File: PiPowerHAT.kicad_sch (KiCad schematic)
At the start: 34 parts

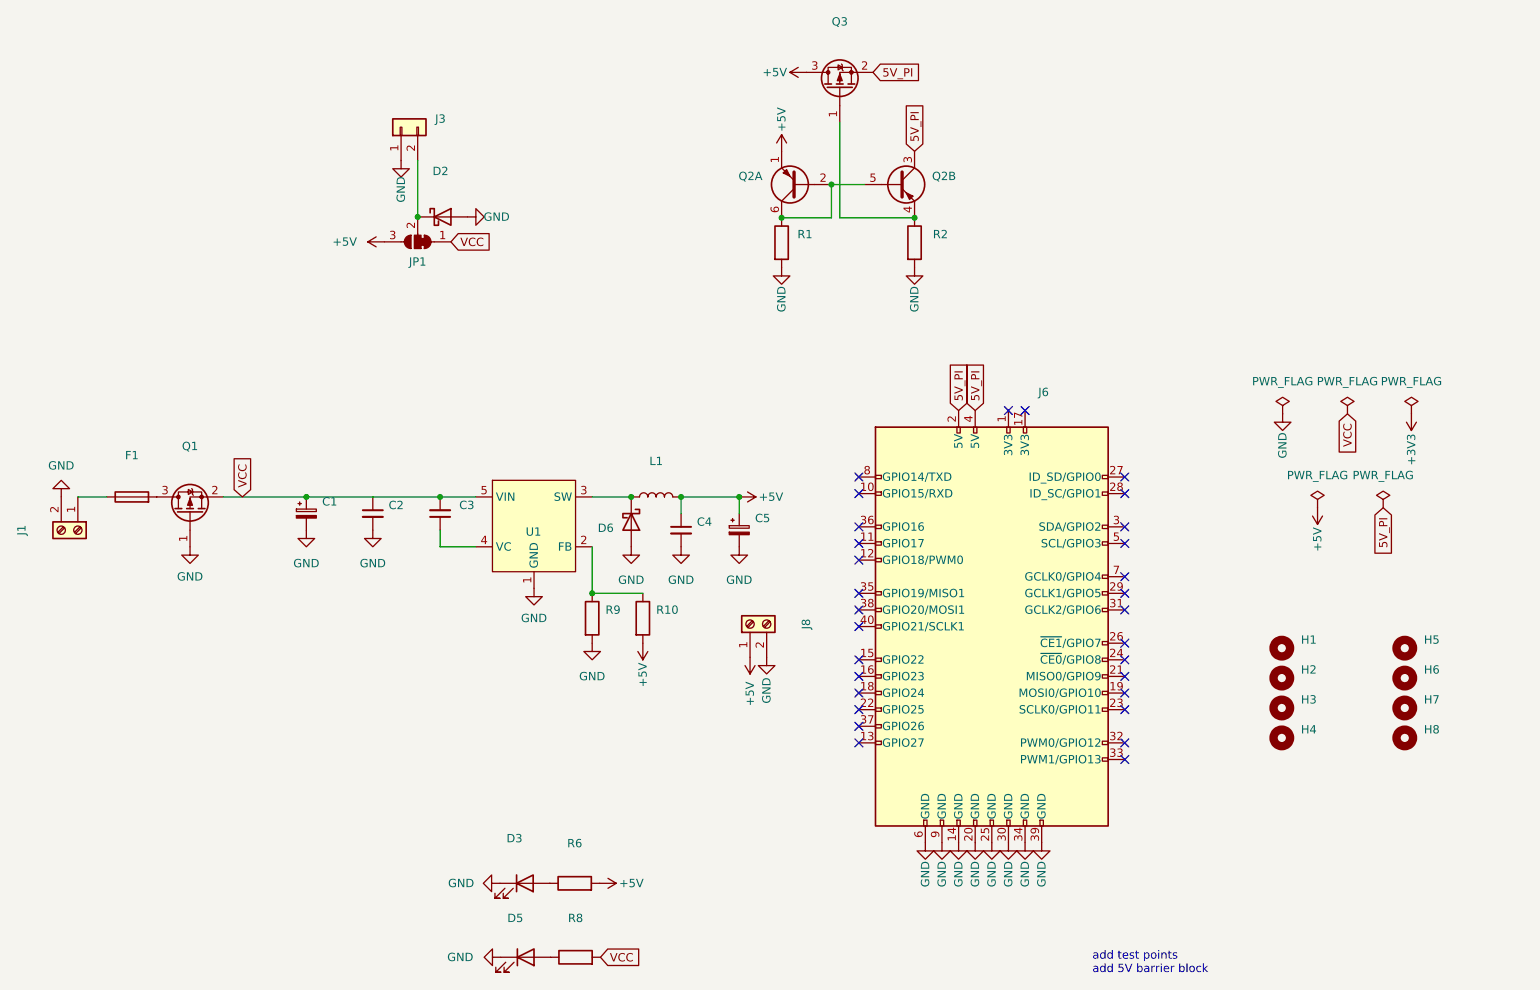
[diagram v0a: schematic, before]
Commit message: Part Numbers for Littelfuse removed.
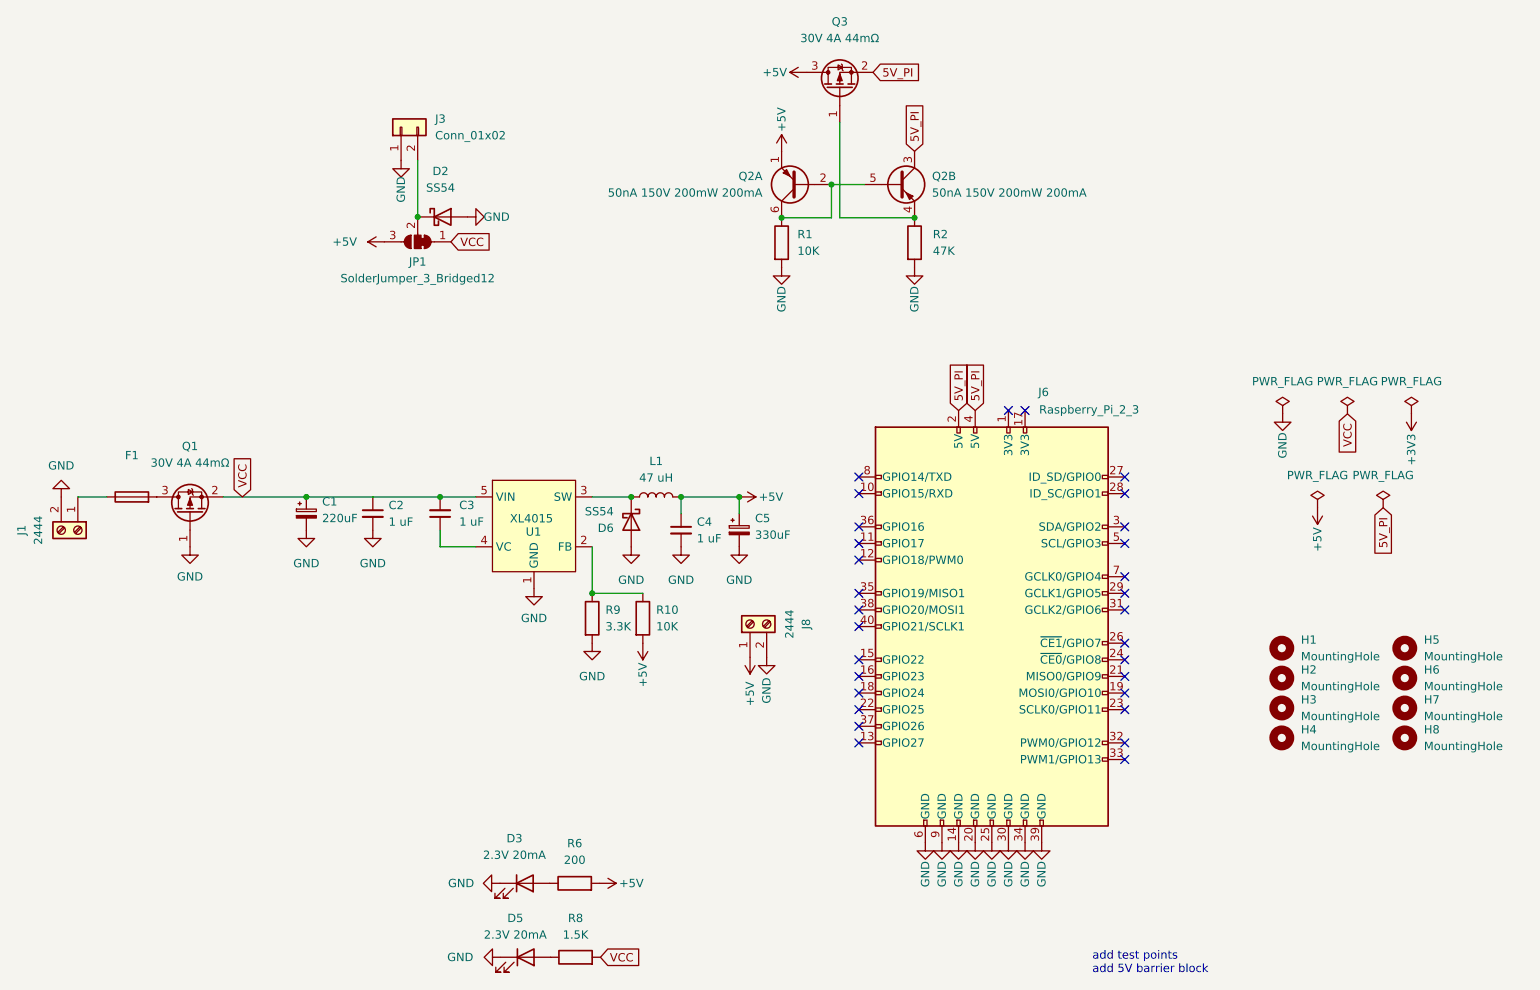
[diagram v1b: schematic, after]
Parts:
- C1: value (none) -> 220uF; footprint (none) -> Capacitor_SMD:CP_Elec_10x10
- C2, C3, C4: value (none) -> 1 uF; footprint (none) -> Capacitor_SMD:C_0603_1608Metric
- C5: value (none) -> 330uF; footprint (none) -> Capacitor_SMD:CP_Elec_6.3x7.7
- D2, D6: value (none) -> SS54; footprint (none) -> Diode_SMD:D_SMA
- D3, D5: value (none) -> 2.3V 20mA; footprint (none) -> LED_SMD:LED_0603_1608Metric
- F1: LCSC C206916 -> (none); PCBway 0154005.DR -> (none)
- H1, H2, H3, H4: value (none) -> MountingHole; footprint (none) -> MountingHole:MountingHole_2.7mm_M2.5_DIN965_Pad
- H5, H6, H7, H8: value (none) -> MountingHole; footprint (none) -> MountingHole:MountingHole_3.5mm
- J1: value (none) -> 2444; footprint (none) -> TerminalBlock_4Ucon:TerminalBlock_4Ucon_1x02_P3.50mm_Horizontal
- J3: value (none) -> Conn_01x02; footprint (none) -> Connector_JST:JST_XH_B2B-XH-A_1x02_P2.50mm_Vertical
- J6: value (none) -> Raspberry_Pi_2_3; footprint (none) -> Connector_PinSocket_2.54mm:PinSocket_2x20_P2.54mm_Vertical
- J8: value (none) -> 2444; footprint (none) -> Connector_JST:JST_XH_B2B-XH-A_1x02_P2.50mm_Vertical
- JP1: value (none) -> SolderJumper_3_Bridged12; footprint (none) -> Jumper:SolderJumper-3_P1.3mm_Bridged2Bar12_RoundedPad1.0x1.5mm
- L1: value (none) -> 47 uH; footprint (none) -> Inductor_SMD:L_12x12mm_H6mm
- Q1, Q3: value (none) -> 30V 4A 44mΩ; footprint (none) -> Package_TO_SOT_SMD:SOT-23
- Q2: value (none) -> 50nA 150V 200mW 200mA; footprint (none) -> Package_TO_SOT_SMD:SOT-363_SC-70-6
- R1: value (none) -> 10K; footprint (none) -> Resistor_SMD:R_0402_1005Metric
- R10: value (none) -> 10K; footprint (none) -> Resistor_SMD:R_0603_1608Metric
- R2: value (none) -> 47K; footprint (none) -> Resistor_SMD:R_0402_1005Metric
- R6: value (none) -> 200; footprint (none) -> Resistor_SMD:R_0402_1005Metric
- R8: value (none) -> 1.5K; footprint (none) -> Resistor_SMD:R_0402_1005Metric
- R9: value (none) -> 3.3K; footprint (none) -> Resistor_SMD:R_0603_1608Metric
- U1: value (none) -> XL4015; footprint (none) -> Package_TO_SOT_SMD:TO-263-5_TabPin3

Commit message: bug fixes
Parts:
- F1: value (none) -> 5A; footprint (none) -> Fuse:Fuseholder_Blade_Mini_Keystone_3568
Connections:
- net 5V_PI: now also Q2.4 (E2); no longer Q2.3 (C2)
- net VCC: now also C2.1
- net at Q3.1 (G), R2.1: now also Q2.3 (C2); no longer Q2.4 (E2)
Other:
- moved on the sheet: Q2B
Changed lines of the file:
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@@
 (kicad_sch (version 20211123) (generator eeschema)
   (paper "A4")
+  (junction (at 137.795 47.879) (diameter 0) (color 0 0 0 0)
+  )
   (junction (at 77.978 95.631) (diameter 0) (color 0 0 0 0)
   )
+  (junction (at 67.7164 95.631) (diameter 0) (color 0 0 0 0)
+  )
   (junction (at 57.531 95.631) (diameter 0) (color 0 0 0 0)
   )
+  (junction (at 107.188 95.631) (diameter 0) (color 0 0 0 0)
+  )
+  (junction (at 114.808 95.631) (diameter 0) (color 0 0 0 0)
+  )
+  (junction (at 123.698 95.631) (diameter 0) (color 0 0 0 0)
+  )
   (junction (at 150.495 52.959) (diameter 0) (color 0 0 0 0)
   )
-  (junction (at 107.188 95.631) (diameter 0) (color 0 0 0 0)
-  )
-  (junction (at 114.808 95.631) (diameter 0) (color 0 0 0 0)
-  )
-  (junction (at 123.698 95.631) (diameter 0) (color 0 0 0 0)
-  )
   (junction (at 130.175 52.959) (diameter 0) (color 0 0 0 0)
-  )
-  (junction (at 137.795 47.879) (diameter 0) (color 0 0 0 0)
   )
   (junction (at 101.219 110.363) (diameter 0) (color 0 0 0 0)
@@
     (stroke (width 0) (type default) (color 0 0 0 0))
   )
+  (wire (pts (xy 158.115 43.053) (xy 158.115 47.879))
+    (stroke (width 0) (type default) (color 0 0 0 0))
+  )
   (wire (pts (xy 101.219 110.363) (xy 108.966 110.363))
     (stroke (width 0) (type default) (color 0 0 0 0))
@@
     (stroke (width 0) (type default) (color 0 0 0 0))
   )
-  (wire (pts (xy 137.795 47.879) (xy 142.875 47.879))
-    (stroke (width 0) (type default) (color 0 0 0 0))
-  )
   (wire (pts (xy 101.219 95.631) (xy 107.188 95.631))
     (stroke (width 0) (type default) (color 0 0 0 0))
   )
+  (wire (pts (xy 137.795 43.053) (xy 158.115 43.053))
+    (stroke (width 0) (type default) (color 0 0 0 0))
+  )
   (wire (pts (xy 77.978 95.631) (xy 83.439 95.631))
     (stroke (width 0) (type default) (color 0 0 0 0))
@@
     (stroke (width 0) (type default) (color 0 0 0 0))
   )
+  (wire (pts (xy 137.795 47.879) (xy 137.795 43.053))
+    (stroke (width 0) (type default) (color 0 0 0 0))
+  )
   (wire (pts (xy 114.808 95.631) (xy 123.698 95.631))
     (stroke (width 0) (type default) (color 0 0 0 0))
@@
     (stroke (width 0) (type default) (color 0 0 0 0))
   )
+  (wire (pts (xy 67.7164 95.631) (xy 77.978 95.631))
+    (stroke (width 0) (type default) (color 0 0 0 0))
+  )
   (wire (pts (xy 74.549 44.196) (xy 74.549 52.832))
     (stroke (width 0) (type default) (color 0 0 0 0))
@@
     (stroke (width 0) (type default) (color 0 0 0 0))
   )
-  (wire (pts (xy 57.531 95.631) (xy 77.978 95.631))
+  (wire (pts (xy 57.531 95.631) (xy 67.7164 95.631))
     (stroke (width 0) (type default) (color 0 0 0 0))
   )
@@
     (pin "1")
   )
-  (symbol (lib_id "power:GND") (at 67.691 100.711 0) (unit 1)
-    (in_bom yes) (on_board yes) (fields_autoplaced)
-    (property "Reference" "#PWR04" (id 0) (at 67.691 107.061 0)
-      (effects (font (size 1.27 1.27)) hide)
-    )
-    (property "Value" "GND" (id 1) (at 67.691 105.791 0))
-    (property "Footprint" "" (id 2) (at 67.691 100.711 0)
-      (effects (font (size 1.27 1.27)) hide)
-    )
-    (property "Datasheet" "" (id 3) (at 67.691 100.711 0)
+  (symbol (lib_id "power:GND") (at 67.7164 100.711 0) (unit 1)
+    (in_bom yes) (on_board yes) (fields_autoplaced)
+    (property "Reference" "#PWR04" (id 0) (at 67.7164 107.061 0)
+      (effects (font (size 1.27 1.27)) hide)
+    )
+    (property "Value" "GND" (id 1) (at 67.7164 105.791 0))
+    (property "Footprint" "" (id 2) (at 67.7164 100.711 0)
+      (effects (font (size 1.27 1.27)) hide)
+    )
+    (property "Datasheet" "" (id 3) (at 67.7164 100.711 0)
       (effects (font (size 1.27 1.27)) hide)
     )
@@
     (pin "1")
   )
-  (symbol (lib_id "Device:C_Small") (at 67.691 98.171 0) (unit 1)
-    (in_bom yes) (on_board yes)
-    (property "Reference" "C2" (id 0) (at 70.104 96.9072 0)
-      (effects (font (size 1.27 1.27)) (justify left))
-    )
-    (property "Value" "1 uF" (id 1) (at 70.104 99.4472 0)
-      (effects (font (size 1.27 1.27)) (justify left))
-    )
-    (property "Footprint" "Capacitor_SMD:C_0603_1608Metric" (id 2) (at 67.691 98.171 0)
-      (effects (font (size 1.27 1.27)) hide)
-    )
-    (property "Datasheet" "~" (id 3) (at 67.691 98.171 0)
-      (effects (font (size 1.27 1.27)) hide)
-    )
-    (property "LCSC" "C15849" (id 4) (at 67.691 98.171 0)
-      (effects (font (size 1.27 1.27)) hide)
-    )
-    (property "PCBway" "CL10A105KB8NNNC" (id 5) (at 67.691 98.171 0)
-      (effects (font (size 1.27 1.27)) hide)
-    )
-    (property "abv.Footprint" "0603" (id 6) (at 67.691 98.171 0)
-      (effects (font (size 1.27 1.27)) hide)
-    )
-    (property "ManfNum" "CL10A105KB8NNNC" (id 7) (at 67.691 98.171 0)
+  (symbol (lib_id "Device:C_Small") (at 67.7164 98.171 0) (unit 1)
+    (in_bom yes) (on_board yes)
+    (property "Reference" "C2" (id 0) (at 70.1294 96.9072 0)
+      (effects (font (size 1.27 1.27)) (justify left))
+    )
+    (property "Value" "1 uF" (id 1) (at 70.1294 99.4472 0)
+      (effects (font (size 1.27 1.27)) (justify left))
+    )
+    (property "Footprint" "Capacitor_SMD:C_0603_1608Metric" (id 2) (at 67.7164 98.171 0)
+      (effects (font (size 1.27 1.27)) hide)
+    )
+    (property "Datasheet" "~" (id 3) (at 67.7164 98.171 0)
+      (effects (font (size 1.27 1.27)) hide)
+    )
+    (property "LCSC" "C15849" (id 4) (at 67.7164 98.171 0)
+      (effects (font (size 1.27 1.27)) hide)
+    )
+    (property "PCBway" "CL10A105KB8NNNC" (id 5) (at 67.7164 98.171 0)
+      (effects (font (size 1.27 1.27)) hide)
+    )
+    (property "abv.Footprint" "0603" (id 6) (at 67.7164 98.171 0)
+      (effects (font (size 1.27 1.27)) hide)
+    )
+    (property "ManfNum" "CL10A105KB8NNNC" (id 7) (at 67.7164 98.171 0)
       (effects (font (size 1.27 1.27)) hide)
     )
@@
     (pin "2")
   )
-  (symbol (lib_id "Transistor_BJT:MMDT5401") (at 147.955 47.879 0) (unit 2)
-    (in_bom yes) (on_board yes) (fields_autoplaced)
-    (property "Reference" "Q2" (id 0) (at 153.162 46.6089 0)
-      (effects (font (size 1.27 1.27)) (justify left))
-    )
-    (property "Value" "50nA 150V 200mW 200mA" (id 1) (at 153.162 49.1489 0)
-      (effects (font (size 1.27 1.27)) (justify left))
-    )
-    (property "Footprint" "Package_TO_SOT_SMD:SOT-363_SC-70-6" (id 2) (at 153.035 45.339 0)
-      (effects (font (size 1.27 1.27)) hide)
-    )
-    (property "Datasheet" "http://www.diodes.com/_files/datasheets/ds30169.pdf" (id 3) (at 147.955 47.879 0)
-      (effects (font (size 1.27 1.27)) hide)
-    )
-    (property "LCSC" "C54540" (id 4) (at 132.715 47.879 0)
-      (effects (font (size 1.27 1.27)) hide)
-    )
-    (property "PCBway" "MMDT5401" (id 5) (at 147.955 47.879 0)
-      (effects (font (size 1.27 1.27)) hide)
-    )
-    (property "abv.Footprint" "SOT-363" (id 6) (at 147.955 47.879 0)
-      (effects (font (size 1.27 1.27)) hide)
-    )
-    (property "ManfNum" "MMDT5401" (id 7) (at 147.955 47.879 0)
+  (symbol (lib_id "Transistor_BJT:MMDT5401") (at 153.035 47.879 180) (unit 2)
+    (in_bom yes) (on_board yes) (fields_autoplaced)
+    (property "Reference" "Q2" (id 0) (at 147.32 46.6089 0)
+      (effects (font (size 1.27 1.27)) (justify left))
+    )
+    (property "Value" "50nA 150V 200mW 200mA" (id 1) (at 147.32 49.1489 0)
+      (effects (font (size 1.27 1.27)) (justify left))
+    )
+    (property "Footprint" "Package_TO_SOT_SMD:SOT-363_SC-70-6" (id 2) (at 147.955 50.419 0)
+      (effects (font (size 1.27 1.27)) hide)
+    )
+    (property "Datasheet" "http://www.diodes.com/_files/datasheets/ds30169.pdf" (id 3) (at 153.035 47.879 0)
+      (effects (font (size 1.27 1.27)) hide)
+    )
+    (property "LCSC" "C54540" (id 4) (at 168.275 47.879 0)
+      (effects (font (size 1.27 1.27)) hide)
+    )
+    (property "PCBway" "MMDT5401" (id 5) (at 153.035 47.879 0)
+      (effects (font (size 1.27 1.27)) hide)
+    )
+    (property "abv.Footprint" "SOT-363" (id 6) (at 153.035 47.879 0)
+      (effects (font (size 1.27 1.27)) hide)
+    )
+    (property "ManfNum" "MMDT5401" (id 7) (at 153.035 47.879 0)
       (effects (font (size 1.27 1.27)) hide)
     )
@@
     (in_bom yes) (on_board yes) (fields_autoplaced)
     (property "Reference" "F1" (id 0) (at 30.861 89.281 90))
-    (property "Value" "" (id 1) (at 30.861 91.821 90))
-    (property "Footprint" "" (id 2) (at 30.861 97.409 90)
-      (effects (font (size 1.27 1.27)) hide)
-    )
+    (property "Value" "5A" (id 1) (at 30.861 91.821 90))
+    (property "Footprint" "Fuse:Fuseholder_Blade_Mini_Keystone_3568" (id 2) (at 30.861 97.409 90)
+      (effects (font (size 1.27 1.27)) hide)
+    )
